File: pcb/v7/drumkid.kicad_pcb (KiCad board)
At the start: 2 copper layers, 90 x 140 mm, 54 parts, among them J1 DIN-5_180degree, J2 DIN-5_180degree, J3 Conn_01x15, J4 Conn_01x15, J9 AudioJack3_Ground_Switch, SW1 SW_Push, SW2 SW_Push, SW3 SW_Push, SW4 SW_Push, SW5 SW_Push, SW6 SW_Push, SW7 SW_SPDT, SW8 SW_SPDT, U1 6N138

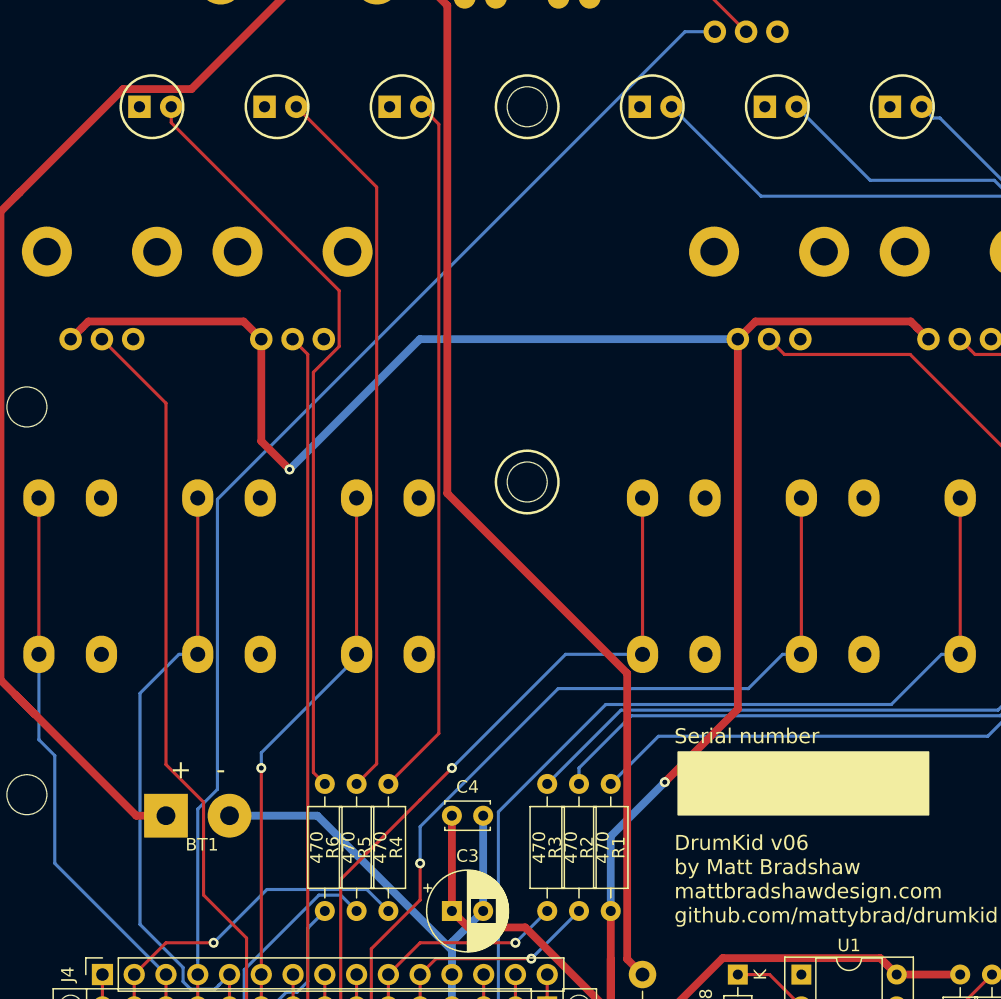
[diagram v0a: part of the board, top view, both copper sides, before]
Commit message: added BOM
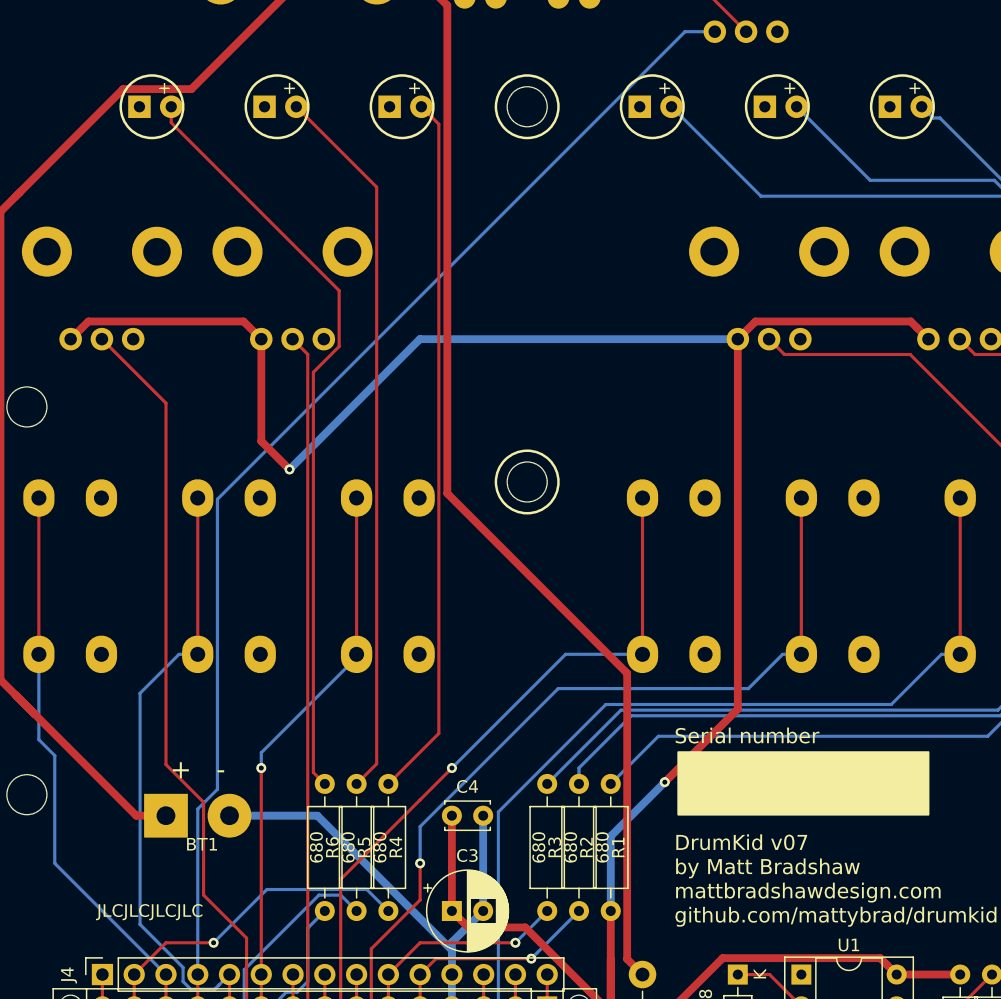
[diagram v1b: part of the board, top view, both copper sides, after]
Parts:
- R1, R2, R3, R4, R5, R6: value 470 -> 680
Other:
- board text added: "(change bank)"
- board text added: "(load)"
- board text added: "(save)"
- board text added: "+"
- board text added: "DrumKid v07 by Matt Bradshaw mattbradshawdesign.com github.com/mattybrad/drumkid"
- board text added: "JLCJLCJLCJLC"
- board text added: "a b c d"
- board text removed: "DrumKid v06 by Matt Bradshaw mattbradshawdesign.com github.com/mattybrad/drumkid"
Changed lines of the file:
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@@
-(kicad_pcb (version 20171130) (host pcbnew "(5.0.1)-3")
+(kicad_pcb (version 20171130) (host pcbnew "(5.1.5)-3")
   (general
     (thickness 1.6)
-    (drawings 51)
+    (drawings 62)
     (tracks 305)
     (zones 0)
@@
   (page A4)
   (layers
-    (0 F.Cu signal)
-    (31 B.Cu signal)
+    (0 F.Cu signal hide)
+    (31 B.Cu signal hide)
     (32 B.Adhes user)
     (33 F.Adhes user)
@@
     (zone_45_only no)
     (trace_min 0.2)
-    (segment_width 0.2)
-    (edge_width 0.2)
     (via_size 0.8)
     (via_drill 0.4)
@@
     (uvia_min_size 0.2)
     (uvia_min_drill 0.1)
+    (edge_width 0.2)
+    (segment_width 0.2)
     (pcb_text_width 0.3)
     (pcb_text_size 1.5 1.5)
@@
       (effects (font (size 1 1) (thickness 0.15)))
     )
-    (fp_text value 470 (at 5.08 0.635 270) (layer F.SilkS)
+    (fp_text value 680 (at 5.08 0.635 270) (layer F.SilkS)
       (effects (font (size 1 1) (thickness 0.15)))
     )
@@
       (effects (font (size 1 1) (thickness 0.15)))
     )
-    (fp_text value 470 (at 5.08 0.635 270) (layer F.SilkS)
+    (fp_text value 680 (at 5.08 0.635 270) (layer F.SilkS)
       (effects (font (size 1 1) (thickness 0.15)))
     )
@@
       (effects (font (size 1 1) (thickness 0.15)))
     )
-    (fp_text value 470 (at 5.08 0.635 270) (layer F.SilkS)
+    (fp_text value 680 (at 5.08 0.635 270) (layer F.SilkS)
       (effects (font (size 1 1) (thickness 0.15)))
     )
@@
       (effects (font (size 1 1) (thickness 0.15)))
     )
-    (fp_text value 470 (at 5.08 0.635 270) (layer F.SilkS)
+    (fp_text value 680 (at 5.08 0.635 270) (layer F.SilkS)
       (effects (font (size 1 1) (thickness 0.15)))
     )
@@
       (effects (font (size 1 1) (thickness 0.15)))
     )
-    (fp_text value 470 (at 5.08 0.635 270) (layer F.SilkS)
+    (fp_text value 680 (at 5.08 0.635 270) (layer F.SilkS)
       (effects (font (size 1 1) (thickness 0.15)))
     )
@@
       (effects (font (size 1 1) (thickness 0.15)))
     )
-    (fp_text value 470 (at 5.08 0.635 270) (layer F.SilkS)
+    (fp_text value 680 (at 5.08 0.635 270) (layer F.SilkS)
       (effects (font (size 1 1) (thickness 0.15)))
     )
@@
     )
   )
+  (gr_text "(change bank)" (at 100.25 97.12) (layer B.SilkS)
+    (effects (font (size 1.5 1.3) (thickness 0.15)) (justify mirror))
+  )
+  (gr_text "(save)" (at 82.5 97.12) (layer B.SilkS)
+    (effects (font (size 1.5 1.3) (thickness 0.15)) (justify mirror))
+  )
+  (gr_text "(load)" (at 118 97.12) (layer B.SilkS)
+    (effects (font (size 1.5 1.3) (thickness 0.15)) (justify mirror))
+  )
+  (gr_text + (at 131 48.5) (layer F.SilkS)
+    (effects (font (size 1 1) (thickness 0.15)))
+  )
+  (gr_text + (at 121 48.5) (layer F.SilkS)
+    (effects (font (size 1 1) (thickness 0.15)))
+  )
+  (gr_text + (at 111 48.5) (layer F.SilkS)
+    (effects (font (size 1 1) (thickness 0.15)))
+  )
+  (gr_text + (at 91 48.5) (layer F.SilkS)
+    (effects (font (size 1 1) (thickness 0.15)))
+  )
+  (gr_text + (at 81 48.5) (layer F.SilkS)
+    (effects (font (size 1 1) (thickness 0.15)))
+  )
+  (gr_text + (at 71 48.5) (layer F.SilkS)
+    (effects (font (size 1 1) (thickness 0.15)))
+  )
+  (gr_text "a\nb\nc\nd" (at 100 73.66) (layer B.SilkS)
+    (effects (font (size 1.2 1.2) (thickness 0.3)) (justify mirror))
+  )
+  (gr_text JLCJLCJLCJLC (at 69.85 114.3) (layer F.SilkS)
+    (effects (font (size 1 1) (thickness 0.15)))
+  )
   (gr_text 6N138 (at 125.73 129.54) (layer F.SilkS)
     (effects (font (size 1 1) (thickness 0.2)))
@@
     (effects (font (size 1.5 1.5) (thickness 0.3)) (justify mirror))
   )
-  (gr_text "DrumKid v06\nby Matt Bradshaw\nmattbradshawdesign.com\ngithub.com/mattybrad/drumkid" (at 111.76 111.76) (layer F.SilkS)
+  (gr_text "DrumKid v07\nby Matt Bradshaw\nmattbradshawdesign.com\ngithub.com/mattybrad/drumkid" (at 111.76 111.76) (layer F.SilkS)
     (effects (font (size 1.2 1.2) (thickness 0.2)) (justify left))
   )
